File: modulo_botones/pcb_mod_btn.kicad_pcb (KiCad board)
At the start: 2 copper layers, 116 x 100 mm, 73 parts, among them J1 leds_1, J10 leds_2, J11 led_3, J12 btn_3, J13 leds_4, J14 leds_4, J15 leds_4, J16 leds_4, J17 btn_4, J18 leds_5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

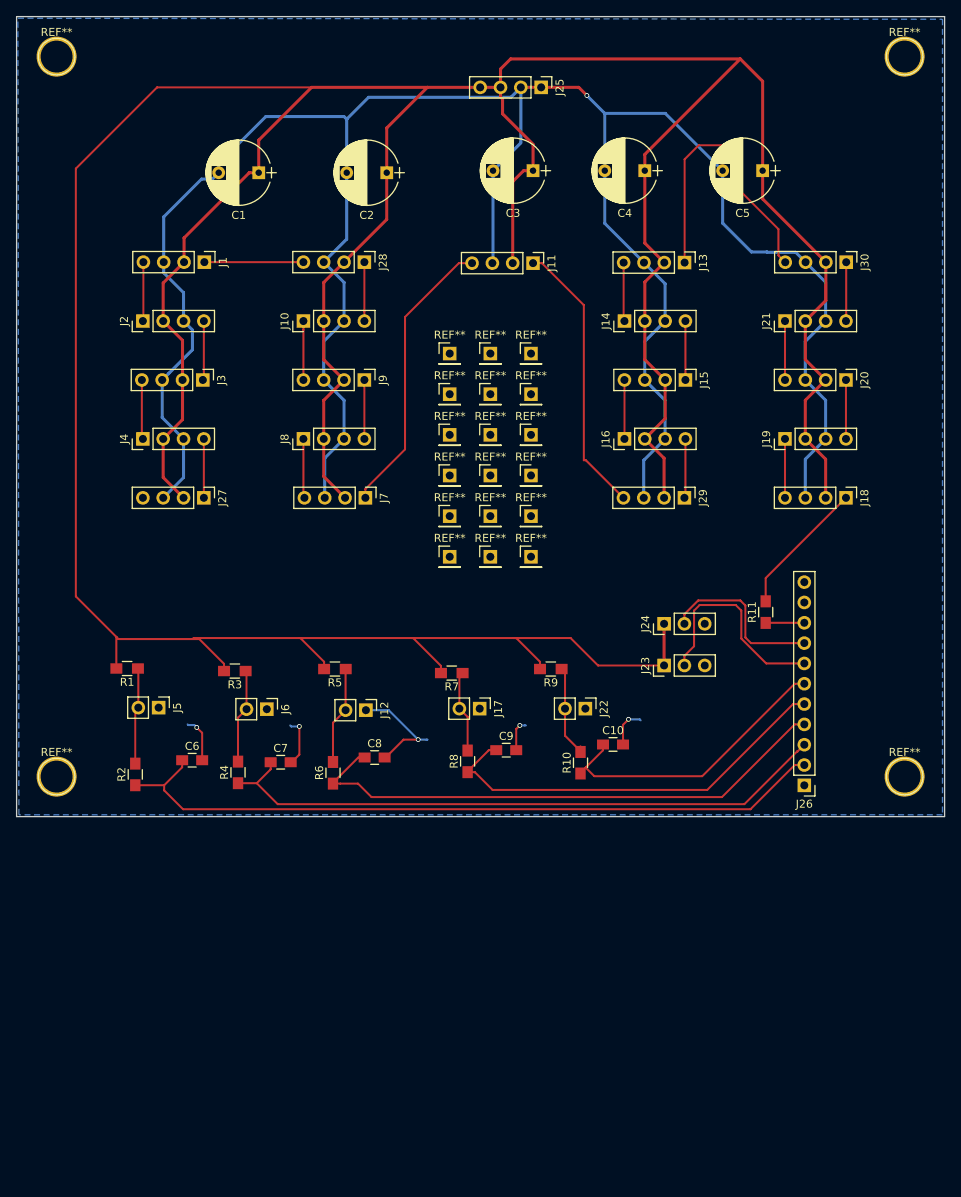
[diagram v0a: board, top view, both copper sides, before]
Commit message: marcas en pin #1 de headers, primer gerber export :3
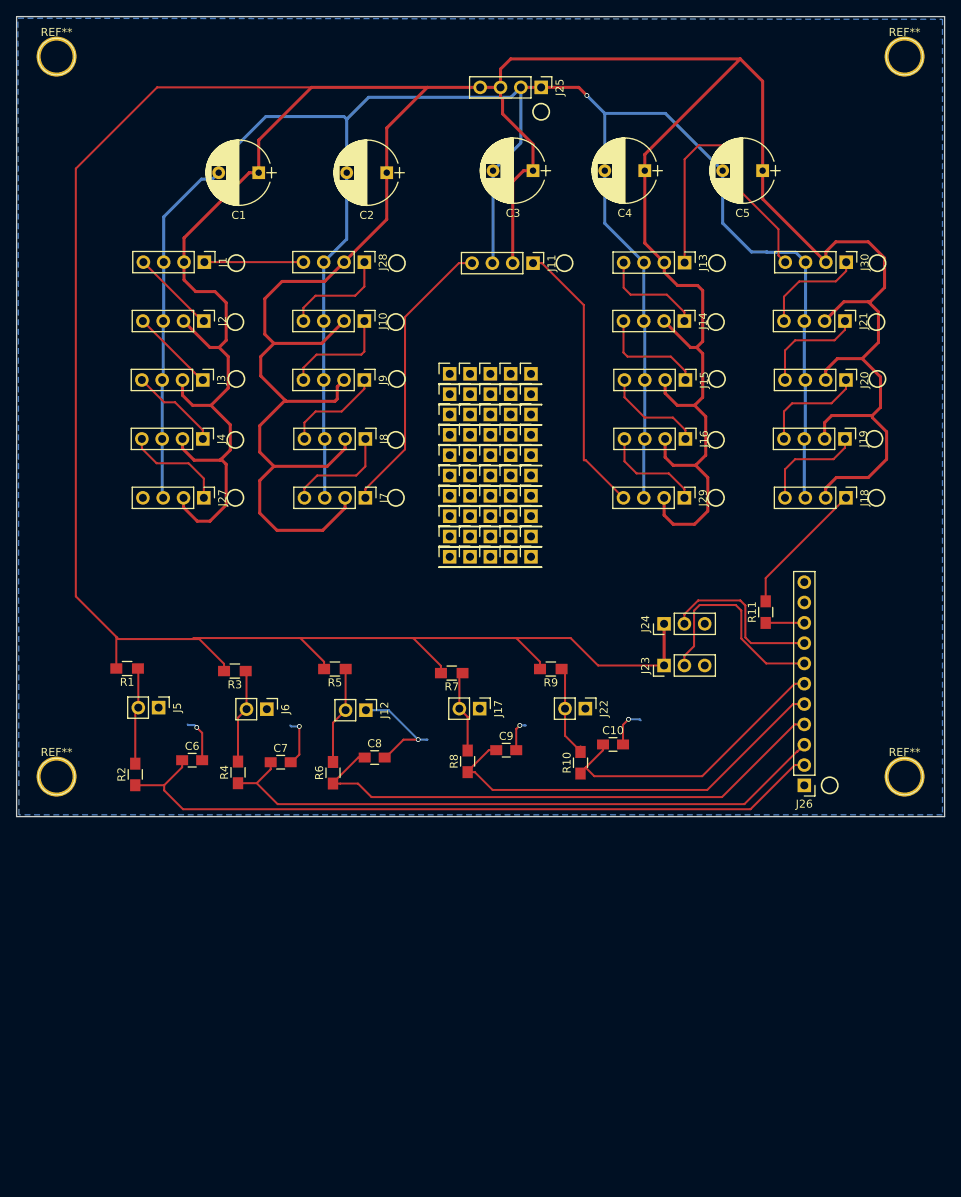
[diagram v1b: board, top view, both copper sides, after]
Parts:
- removed the REF** at (114.3, 96.5)
- removed the REF** at (109.2, 86.4)
- removed the REF** at (104.1, 86.4)
- removed the REF** at (114.3, 86.4)
- removed the REF** at (114.3, 76.2)
- removed the REF** at (104.1, 76.2)
- removed the REF** at (109.2, 76.2)
- removed the REF** at (109.2, 71.1)
- removed the REF** at (104.1, 71.1)
- removed the REF** at (114.3, 71.1)
- removed the REF** at (109.2, 96.5)
- removed the REF** at (109.2, 91.4)
- removed the REF** at (104.1, 91.4)
- removed the REF** at (114.3, 91.4)
- removed the REF** at (114.3, 81.3)
- removed the REF** at (104.1, 81.3)
- removed the REF** at (109.2, 81.3)
- added ?: , Pin_Headers:Pin_Header_Straight_1x01_Pitch2.54mm, F.Cu at (104.1, 76.2)
- added ?: , Pin_Headers:Pin_Header_Straight_1x01_Pitch2.54mm, F.Cu at (114.3, 73.7)
- added ?: , Pin_Headers:Pin_Header_Straight_1x01_Pitch2.54mm, F.Cu at (104.1, 86.4)
- added ?: , Pin_Headers:Pin_Header_Straight_1x01_Pitch2.54mm, F.Cu at (106.7, 86.4)
- added ?: , Pin_Headers:Pin_Header_Straight_1x01_Pitch2.54mm, F.Cu at (106.7, 83.8)
- added ?: , Pin_Headers:Pin_Header_Straight_1x01_Pitch2.54mm, F.Cu at (104.1, 83.8)
- added ?: , Pin_Headers:Pin_Header_Straight_1x01_Pitch2.54mm, F.Cu at (109.2, 83.8)
- added ?: , Pin_Headers:Pin_Header_Straight_1x01_Pitch2.54mm, F.Cu at (111.8, 83.8)
- added ?: , Pin_Headers:Pin_Header_Straight_1x01_Pitch2.54mm, F.Cu at (111.8, 86.4)
- added ?: , Pin_Headers:Pin_Header_Straight_1x01_Pitch2.54mm, F.Cu at (109.2, 86.4)
- added ?: , Pin_Headers:Pin_Header_Straight_1x01_Pitch2.54mm, F.Cu at (114.3, 86.4)
- added ?: , Pin_Headers:Pin_Header_Straight_1x01_Pitch2.54mm, F.Cu at (106.7, 76.2)
- added ?: , Pin_Headers:Pin_Header_Straight_1x01_Pitch2.54mm, F.Cu at (114.3, 83.8)
- added ?: , Pin_Headers:Pin_Header_Straight_1x01_Pitch2.54mm, F.Cu at (114.3, 78.7)
- added ?: , Pin_Headers:Pin_Header_Straight_1x01_Pitch2.54mm, F.Cu at (114.3, 81.3)
- added ?: , Pin_Headers:Pin_Header_Straight_1x01_Pitch2.54mm, F.Cu at (109.2, 81.3)
- added ?: , Pin_Headers:Pin_Header_Straight_1x01_Pitch2.54mm, F.Cu at (111.8, 81.3)
- added ?: , Pin_Headers:Pin_Header_Straight_1x01_Pitch2.54mm, F.Cu at (111.8, 78.7)
- added ?: , Pin_Headers:Pin_Header_Straight_1x01_Pitch2.54mm, F.Cu at (109.2, 78.7)
- added ?: , Pin_Headers:Pin_Header_Straight_1x01_Pitch2.54mm, F.Cu at (104.1, 78.7)
- added ?: , Pin_Headers:Pin_Header_Straight_1x01_Pitch2.54mm, F.Cu at (106.7, 78.7)
- added ?: , Pin_Headers:Pin_Header_Straight_1x01_Pitch2.54mm, F.Cu at (106.7, 81.3)
- added ?: , Pin_Headers:Pin_Header_Straight_1x01_Pitch2.54mm, F.Cu at (106.7, 73.7)
- added ?: , Pin_Headers:Pin_Header_Straight_1x01_Pitch2.54mm, F.Cu at (104.1, 81.3)
- added ?: , Pin_Headers:Pin_Header_Straight_1x01_Pitch2.54mm, F.Cu at (104.1, 91.4)
- added ?: , Pin_Headers:Pin_Header_Straight_1x01_Pitch2.54mm, F.Cu at (106.7, 91.4)
- added ?: , Pin_Headers:Pin_Header_Straight_1x01_Pitch2.54mm, F.Cu at (106.7, 88.9)
- added ?: , Pin_Headers:Pin_Header_Straight_1x01_Pitch2.54mm, F.Cu at (104.1, 88.9)
- added ?: , Pin_Headers:Pin_Header_Straight_1x01_Pitch2.54mm, F.Cu at (109.2, 88.9)
- added ?: , Pin_Headers:Pin_Header_Straight_1x01_Pitch2.54mm, F.Cu at (111.8, 88.9)
- added ?: , Pin_Headers:Pin_Header_Straight_1x01_Pitch2.54mm, F.Cu at (111.8, 91.4)
- added ?: , Pin_Headers:Pin_Header_Straight_1x01_Pitch2.54mm, F.Cu at (109.2, 91.4)
- added ?: , Pin_Headers:Pin_Header_Straight_1x01_Pitch2.54mm, F.Cu at (114.3, 91.4)
- added ?: , Pin_Headers:Pin_Header_Straight_1x01_Pitch2.54mm, F.Cu at (104.1, 73.7)
- added ?: , Pin_Headers:Pin_Header_Straight_1x01_Pitch2.54mm, F.Cu at (114.3, 88.9)
- added ?: , Pin_Headers:Pin_Header_Straight_1x01_Pitch2.54mm, F.Cu at (114.3, 94.0)
- added ?: , Pin_Headers:Pin_Header_Straight_1x01_Pitch2.54mm, F.Cu at (114.3, 96.5)
- added ?: , Pin_Headers:Pin_Header_Straight_1x01_Pitch2.54mm, F.Cu at (109.2, 96.5)
- added ?: , Pin_Headers:Pin_Header_Straight_1x01_Pitch2.54mm, F.Cu at (111.8, 96.5)
- added ?: , Pin_Headers:Pin_Header_Straight_1x01_Pitch2.54mm, F.Cu at (111.8, 94.0)
- added ?: , Pin_Headers:Pin_Header_Straight_1x01_Pitch2.54mm, F.Cu at (109.2, 94.0)
- added ?: , Pin_Headers:Pin_Header_Straight_1x01_Pitch2.54mm, F.Cu at (104.1, 94.0)
- added ?: , Pin_Headers:Pin_Header_Straight_1x01_Pitch2.54mm, F.Cu at (106.7, 94.0)
- added ?: , Pin_Headers:Pin_Header_Straight_1x01_Pitch2.54mm, F.Cu at (106.7, 96.5)
- added ?: , Pin_Headers:Pin_Header_Straight_1x01_Pitch2.54mm, F.Cu at (109.2, 73.7)
- added ?: , Pin_Headers:Pin_Header_Straight_1x01_Pitch2.54mm, F.Cu at (111.8, 73.7)
- added ?: , Pin_Headers:Pin_Header_Straight_1x01_Pitch2.54mm, F.Cu at (111.8, 76.2)
- added ?: , Pin_Headers:Pin_Header_Straight_1x01_Pitch2.54mm, F.Cu at (109.2, 76.2)
- added ?: , Pin_Headers:Pin_Header_Straight_1x01_Pitch2.54mm, F.Cu at (114.3, 76.2)
- moved J8 7.75 mm to (93.6, 81.8), turned to 270 degrees
- moved J16 7.62 mm to (133.6, 81.8), turned to 270 degrees
- moved J2 7.62 mm to (73.4, 67.1), turned to 270 degrees
- moved J10 7.62 mm to (93.5, 67.1), turned to 270 degrees
- moved J14 7.49 mm to (133.5, 67.1), turned to 270 degrees
- moved J19 7.49 mm to (153.5, 81.8), turned to 270 degrees
- moved J21 7.49 mm to (153.5, 67.1), turned to 270 degrees
- moved J4 7.49 mm to (73.3, 81.8), turned to 270 degrees
- renumbered REF** to ?
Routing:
- net +5V: track 529.3 -> 682.1 mm
- net GND: track 340.6 -> 323.3 mm
- net Net-(J10-Pad1): track 7.37 -> 13.8 mm
- net Net-(J14-Pad4): track 7.37 -> 13.8 mm
- net Net-(J7-Pad4): track 7.42 -> 13.6 mm
- net Net-(J19-Pad4): track 7.37 -> 13.5 mm
- net Net-(J10-Pad4): track 7.37 -> 13.4 mm
- net Net-(J20-Pad4): track 7.37 -> 13.4 mm
- net Net-(J18-Pad4): track 7.37 -> 13.3 mm
- net Net-(J21-Pad4): track 7.37 -> 13.3 mm
- net Net-(J13-Pad4): track 7.36 -> 13.1 mm
- net Net-(J16-Pad4): track 7.42 -> 13.0 mm
- net Net-(J27-Pad1): track 7.37 -> 12.9 mm
- net Net-(J15-Pad4): track 7.37 -> 12.6 mm
- net Net-(J8-Pad4): track 7.37 -> 12.4 mm
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
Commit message: marcas pines, reemplazo borneras, orientacion, separacion headers, ubicacion arduino
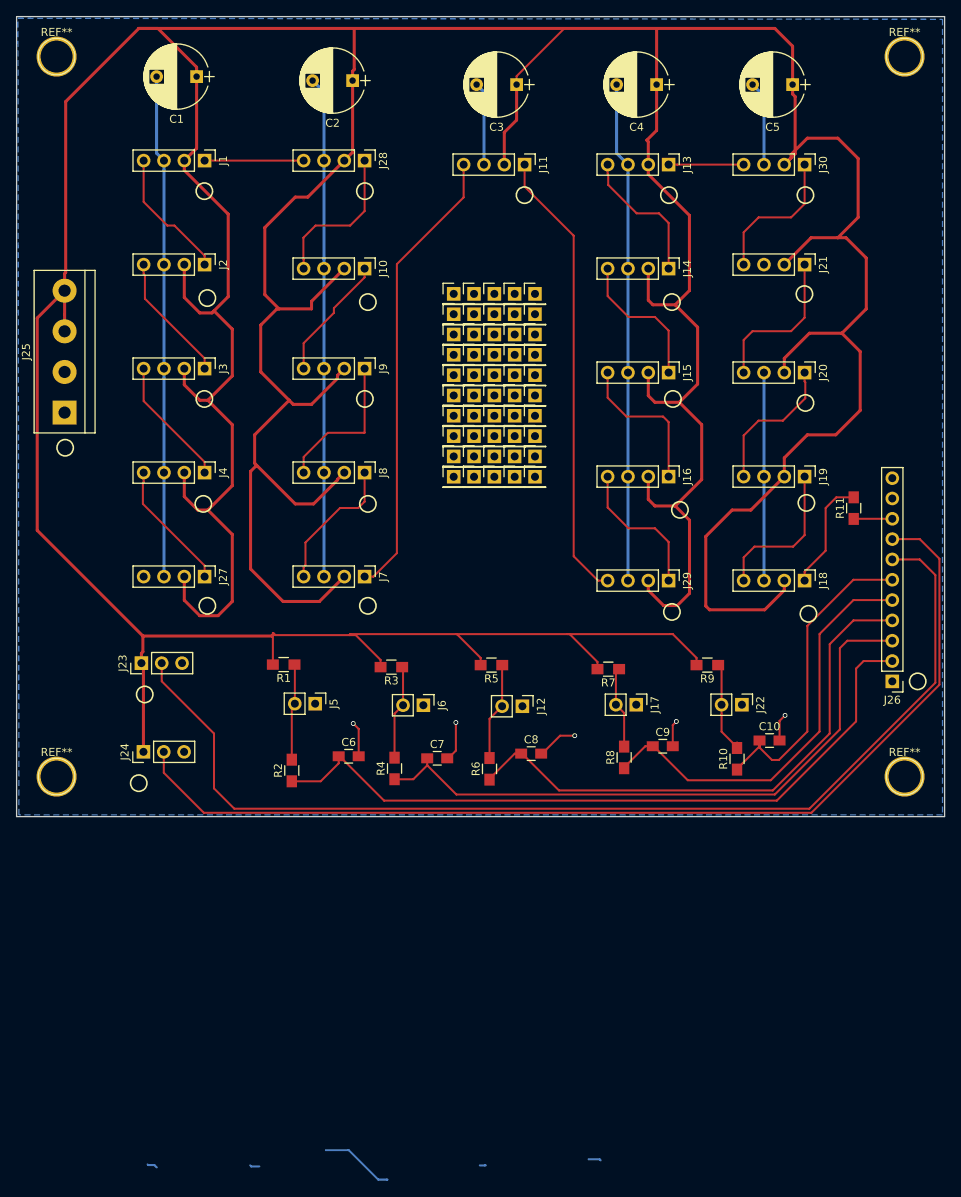
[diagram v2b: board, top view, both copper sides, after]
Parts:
- J25: footprint Pin_Headers:Pin_Header_Straight_1x04_Pitch2.54mm -> Connectors_Terminal_Blocks:TerminalBlock_bornier-4_P5.08mm
- moved J25 72.1 mm to (56.0, 78.5), turned to 90 degrees
- moved J24 67.0 mm to (65.9, 120.9)
- moved J23 65.3 mm to (65.6, 109.8)
- moved J22 19.6 mm to (140.7, 115.0)
- moved C6 19.6 mm to (91.5, 121.5)
- moved J12 19.6 mm to (113.2, 115.2)
- moved J17 19.6 mm to (127.5, 115.0)
- moved J5 19.6 mm to (87.3, 114.9)
- moved J6 19.6 mm to (100.8, 115.1)
- moved R2 19.6 mm to (84.4, 123.2)
- moved R3 19.6 mm to (96.8, 110.3)
- moved R4 19.6 mm to (97.2, 123.0)
- moved R5 19.6 mm to (109.4, 110.1)
- moved R6 19.6 mm to (109.1, 123.0)
- moved R8 19.6 mm to (125.9, 121.6)
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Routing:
- net +5V: track 682.1 -> 798.3 mm
- net /pot_2: track 21.4 -> 130.9 mm
- net /pot_1: track 26.5 -> 135.8 mm
- net GND: track 323.3 -> 256.2 mm, vias 6 -> 5
- net /leds_5: track 36.7 -> 9.38 mm
- net /leds_4: track 34.8 -> 57.0 mm
- net /leds_3: track 35.8 -> 57.3 mm
- net (no net): track 0.00 -> 14.2 mm
- net Net-(J8-Pad4): track 12.4 -> 18.8 mm
- net Net-(J15-Pad4): track 12.6 -> 18.8 mm
- net Net-(J20-Pad4): track 13.4 -> 19.5 mm
- net Net-(J1-Pad4): track 10.6 -> 16.7 mm
- net Net-(J10-Pad4): track 13.4 -> 19.2 mm
- net Net-(J18-Pad4): track 13.3 -> 19.0 mm
- net Net-(J2-Pad4): track 10.7 -> 16.2 mm
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
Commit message: marcas botones ok, gerber exports ultima version
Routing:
- net (no net): track 14.2 -> 0.00 mm
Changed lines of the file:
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@@
     (links 119)
     (no_connects 0)
-    (area 49.924999 28.924999 166.075001 129.075001)
+    (area 27.435716 19.3 181.135715 142.700001)
     (thickness 1.6)
-    (drawings 33)
-    (tracks 433)
+    (drawings 38)
+    (tracks 420)
     (zones 0)
     (modules 105)
@@
   )
   (setup
-    (last_trace_width 0.254)
+    (last_trace_width 0.25)
     (user_trace_width 0.1524)
     (user_trace_width 0.254)
@@
     (visible_elements FFFFFF7F)
     (pcbplotparams
-      (layerselection 0x01030_80000001)
+      (layerselection 0x31030_80000001)
       (usegerberextensions false)
       (excludeedgelayer true)
@@
     )
   )
+  (gr_circle (center 140.645 111.798) (end 140.772 112.814) (layer F.SilkS) (width 0.2))
+  (gr_circle (center 127.691 111.798) (end 127.818 112.814) (layer F.SilkS) (width 0.2))
+  (gr_circle (center 113.467 112.052) (end 113.594 113.068) (layer F.SilkS) (width 0.2))
+  (gr_circle (center 100.767 111.798) (end 100.894 112.814) (layer F.SilkS) (width 0.2))
+  (gr_circle (center 87.305 111.798) (end 87.432 112.814) (layer F.SilkS) (width 0.2))
   (gr_circle (center 66.016 113.731) (end 66.143 114.747) (layer F.SilkS) (width 0.2))
   (gr_circle (center 65.27 124.821) (end 65.397 125.837) (layer F.SilkS) (width 0.2))
@@
   (gr_line (start 166 29) (end 166 129) (angle 90) (layer Edge.Cuts) (width 0.15))
   (gr_line (start 50 29) (end 166 29) (angle 90) (layer Edge.Cuts) (width 0.15))
-  (segment (start 79.328 172.729) (end 79.201 172.602) (width 0.254) (layer B.Cu) (net 0))
-  (segment (start 80.344 172.729) (end 79.328 172.729) (width 0.254) (layer B.Cu) (net 0))
-  (segment (start 66.374 172.475) (end 66.455001 172.556001) (width 0.254) (layer B.Cu) (net 0))
-  (segment (start 67.517 172.856) (end 67.217001 172.556001) (width 0.254) (layer B.Cu) (net 0))
-  (segment (start 67.217001 172.556001) (end 66.455001 172.556001) (width 0.254) (layer B.Cu) (net 0))
-  (segment (start 123.016 171.967) (end 122.889 171.84) (width 0.254) (layer B.Cu) (net 0))
-  (segment (start 121.492 171.84) (end 122.889 171.84) (width 0.254) (layer B.Cu) (net 0))
-  (segment (start 107.903 172.602) (end 108.538 172.602) (width 0.254) (layer B.Cu) (net 0))
-  (segment (start 108.665 172.602) (end 108.538 172.602) (width 0.254) (layer B.Cu) (net 0))
-  (segment (start 88.6625 170.697) (end 91.52 170.697) (width 0.254) (layer B.Cu) (net 0))
-  (segment (start 91.52 170.697) (end 95.203 174.38) (width 0.254) (layer B.Cu) (net 0))
-  (segment (start 95.203 174.38) (end 96.346 174.38) (width 0.254) (layer B.Cu) (net 0))
-  (segment (start 96.219 174.38) (end 96.346 174.38) (width 0.254) (layer B.Cu) (net 0))
   (segment (start 154.94 110.49) (end 155.875 109.555) (width 0.254) (layer F.Cu) (net 1))
   (segment (start 155.875 109.555) (end 159.463 109.555) (width 0.254) (layer F.Cu) (net 1))
